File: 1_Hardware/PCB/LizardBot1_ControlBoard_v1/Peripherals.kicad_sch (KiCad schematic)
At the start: 30 parts, among them J501 Conn_01x03, J502 Conn_01x02, Q501 AO3400A, Q502 BSS138, Q503 BSS138, Q504 AO3400A, SW501 SW_Push, U501 MIC5225, U502 ICM-20948

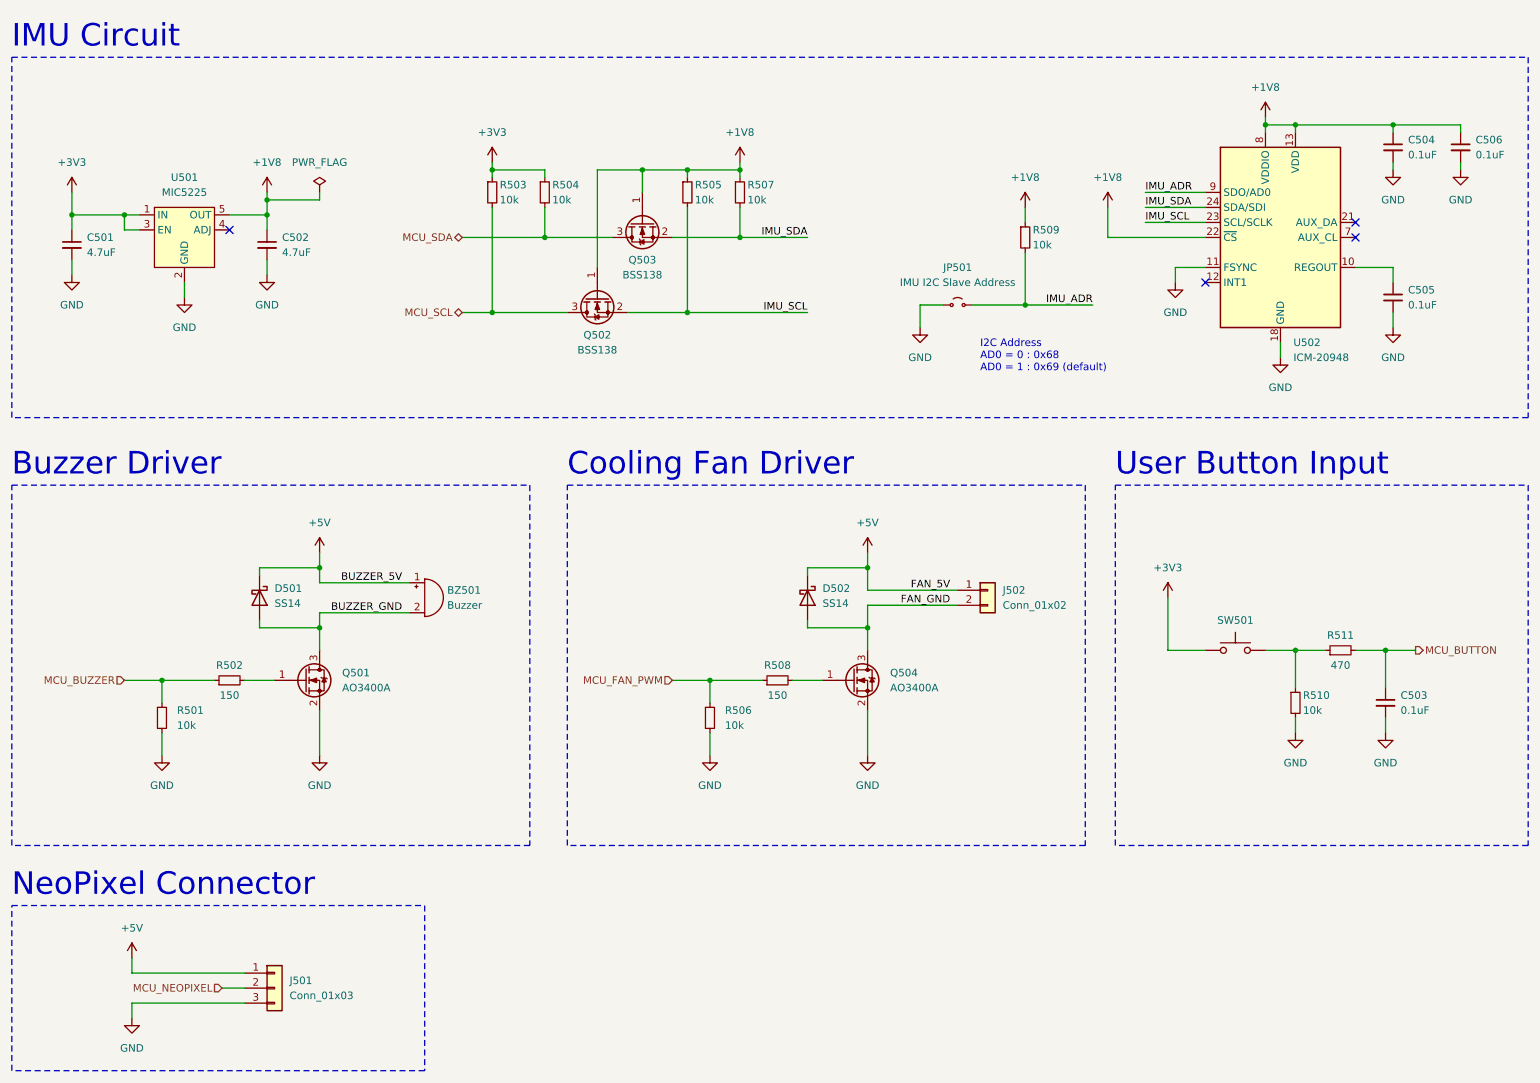
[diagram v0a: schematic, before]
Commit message: Added Communication_Interfaces schematic
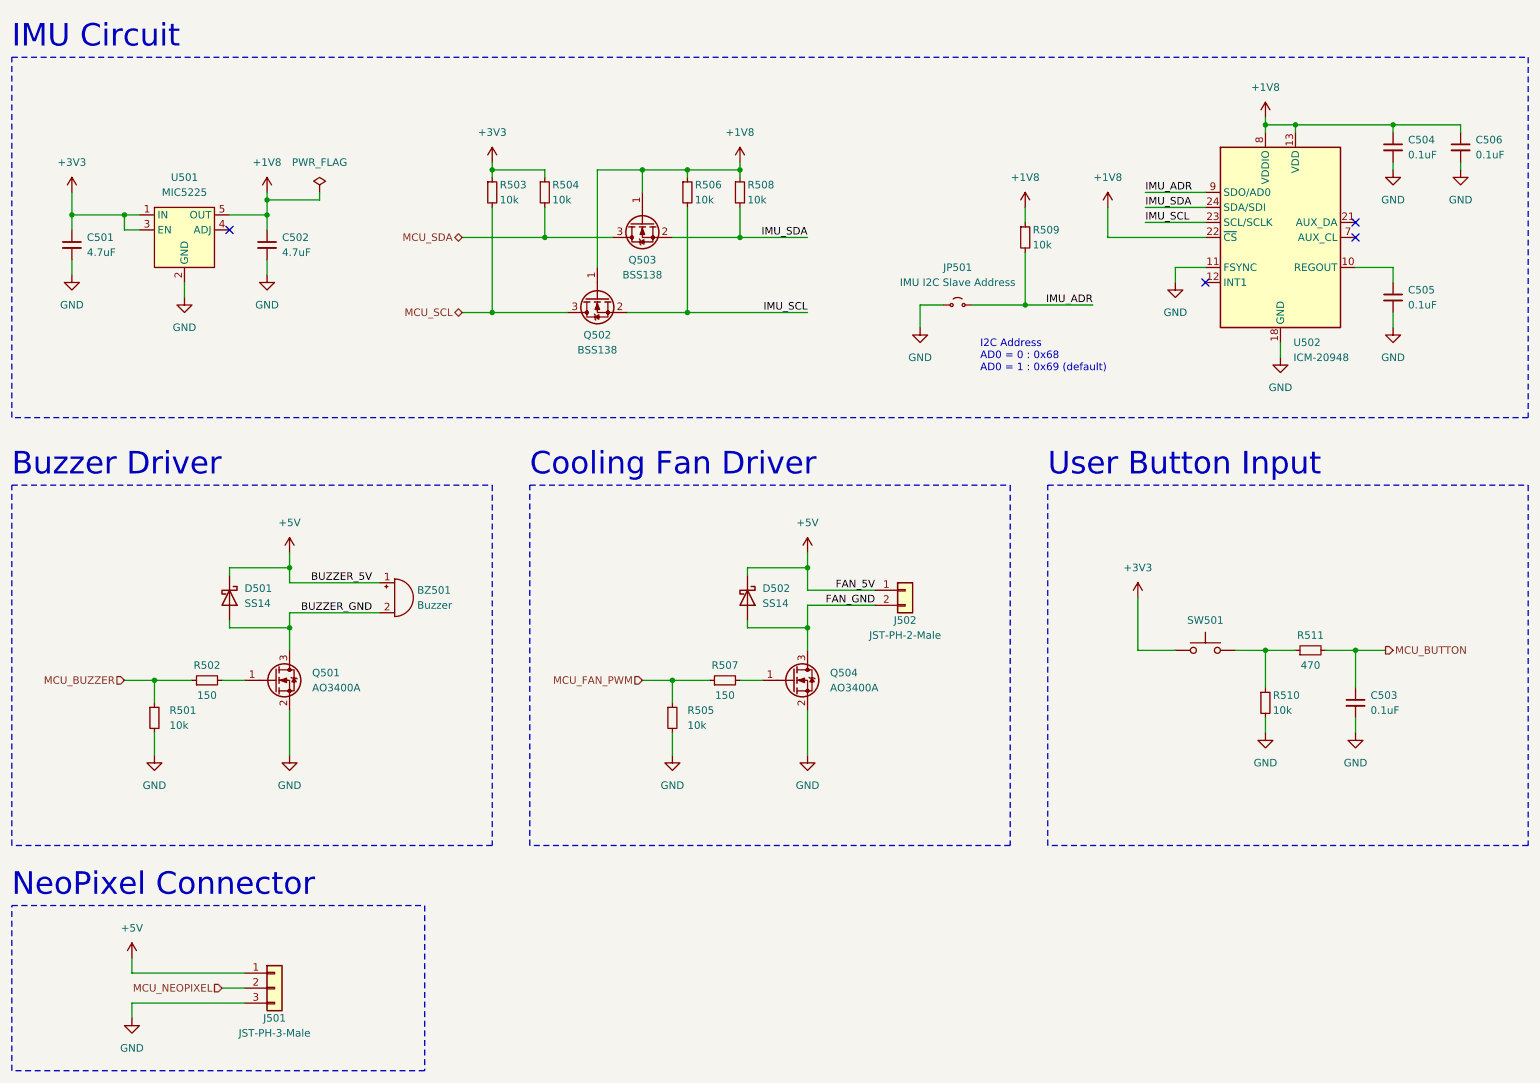
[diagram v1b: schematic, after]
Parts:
- removed R506: 10k, symbol Device:R_Small
- removed R508: 150, symbol Device:R_Small
- added R505: 10k, symbol Device:R_Small
- added R507: 150, symbol Device:R_Small
- J501: value Conn_01x03 -> JST-PH-3-Male
- J502: value Conn_01x02 -> JST-PH-2-Male
- renumbered R505 to R506, R507 to R508
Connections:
- net GND: now also R505.2
- net MCU_FAN_PWM: now also R505.1, R507.1
- net at Q504.1 (G): now also R507.2
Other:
- moved on the sheet: BZ501, C503, D501, D502, J502, Q501, Q504, R501, R502, R510, R511, SW501

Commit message: PCB schematics revision
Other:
- title: LizardBot 1 Control Board: Outputs -> LizardBot 1 Control Board: Peripherals

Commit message: Updated schematics. Assigned footprints. Added BOM to /4_Docs.
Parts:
- BZ501: footprint (none) -> Buzzer_Beeper:Buzzer_12x9.5RM7.6
- C501, C502: footprint (none) -> Capacitor_SMD:C_0805_2012Metric_Pad1.18x1.45mm_HandSolder
- C503, C504, C505, C506: footprint (none) -> Capacitor_SMD:C_0603_1608Metric_Pad1.08x0.95mm_HandSolder
- J501: footprint (none) -> Connector_JST:JST_PH_S3B-PH-K_1x03_P2.00mm_Horizontal
- J502: footprint (none) -> Connector_JST:JST_PH_S2B-PH-K_1x02_P2.00mm_Horizontal
- JP501: footprint (none) -> Jumper:SolderJumper-2_P1.3mm_Open_TrianglePad1.0x1.5mm
- R501, R502, R505, R507: footprint (none) -> Resistor_SMD:R_0805_2012Metric_Pad1.20x1.40mm_HandSolder
- R503, R504, R506, R508, R509, R510, R511: footprint (none) -> Resistor_SMD:R_0603_1608Metric_Pad0.98x0.95mm_HandSolder
- SW501: footprint (none) -> Button_Switch_THT:SW_PUSH-12mm
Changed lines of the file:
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@@
 			)
 		)
-		(property "Footprint" ""
+		(property "Footprint" "Buzzer_Beeper:Buzzer_12x9.5RM7.6"
 			(at 84.455 111.76 90)
 			(effects
@@
 			)
 		)
-		(property "Footprint" ""
+		(property "Footprint" "Resistor_SMD:R_0603_1608Metric_Pad0.98x0.95mm_HandSolder"
 			(at 240.03 123.19 0)
 			(effects
@@
 			)
 		)
-		(property "Footprint" ""
+		(property "Footprint" "Capacitor_SMD:C_0603_1608Metric_Pad1.08x0.95mm_HandSolder"
 			(at 254 38.1 0)
 			(effects
@@
 			)
 		)
-		(property "Footprint" ""
+		(property "Footprint" "Jumper:SolderJumper-2_P1.3mm_Open_TrianglePad1.0x1.5mm"
 			(at 180.34 64.77 0)
 			(effects
@@
 			)
 		)
-		(property "Footprint" ""
+		(property "Footprint" "Resistor_SMD:R_0603_1608Metric_Pad0.98x0.95mm_HandSolder"
 			(at 232.41 132.08 0)
 			(effects
@@
 			)
 		)
-		(property "Footprint" ""
+		(property "Footprint" "Button_Switch_THT:SW_PUSH-12mm"
 			(at 222.25 118.11 0)
 			(effects
@@
 			)
 		)
-		(property "Footprint" ""
+		(property "Footprint" "Capacitor_SMD:C_0603_1608Metric_Pad1.08x0.95mm_HandSolder"
 			(at 247.65 132.08 0)
 			(effects
@@
 			)
 		)
-		(property "Footprint" ""
+		(property "Footprint" "Resistor_SMD:R_0805_2012Metric_Pad1.20x1.40mm_HandSolder"
 			(at 140.97 128.27 0)
 			(effects
@@
 			)
 		)
-		(property "Footprint" ""
+		(property "Footprint" "Resistor_SMD:R_0603_1608Metric_Pad0.98x0.95mm_HandSolder"
 			(at 110.49 45.72 0)
 			(effects
@@
 			)
 		)
-		(property "Footprint" ""
+		(property "Footprint" "Capacitor_SMD:C_0805_2012Metric_Pad1.18x1.45mm_HandSolder"
 			(at 30.48 54.61 0)
 			(effects
@@
 			)
 		)
-		(property "Footprint" ""
+		(property "Footprint" "Resistor_SMD:R_0603_1608Metric_Pad0.98x0.95mm_HandSolder"
 			(at 191.77 53.34 0)
 			(effects
@@
 			)
 		)
-		(property "Footprint" ""
+		(property "Footprint" "Resistor_SMD:R_0603_1608Metric_Pad0.98x0.95mm_HandSolder"
 			(at 134.62 45.72 0)
 			(effects
@@
 			)
 		)
-		(property "Footprint" ""
+		(property "Footprint" "Resistor_SMD:R_0603_1608Metric_Pad0.98x0.95mm_HandSolder"
 			(at 101.6 45.72 0)
 			(effects
@@
 			)
 		)
-		(property "Footprint" ""
+		(property "Footprint" "Resistor_SMD:R_0805_2012Metric_Pad1.20x1.40mm_HandSolder"
 			(at 53.34 128.27 0)
 			(effects
@@
 			)
 		)
-		(property "Footprint" ""
+		(property "Footprint" "Connector_JST:JST_PH_S3B-PH-K_1x03_P2.00mm_Horizontal"
 			(at 64.77 180.34 0)
 			(effects
@@
 			)
 		)
-		(property "Footprint" ""
+		(property "Footprint" "Connector_JST:JST_PH_S2B-PH-K_1x02_P2.00mm_Horizontal"
 			(at 171.45 113.03 0)
 			(effects
@@
 			)
 		)
-		(property "Footprint" ""
+		(property "Footprint" "Resistor_SMD:R_0805_2012Metric_Pad1.20x1.40mm_HandSolder"
 			(at 44.45 134.62 0)
 			(effects
@@
 			)
 		)
-		(property "Footprint" ""
+		(property "Footprint" "Capacitor_SMD:C_0805_2012Metric_Pad1.18x1.45mm_HandSolder"
 			(at 63.5 54.61 0)
 			(effects
@@
 			)
 		)
-		(property "Footprint" ""
+		(property "Footprint" "Resistor_SMD:R_0805_2012Metric_Pad1.20x1.40mm_HandSolder"
 			(at 132.08 134.62 0)
 			(effects
@@
 			)
 		)
-		(property "Footprint" ""
+		(property "Footprint" "Capacitor_SMD:C_0603_1608Metric_Pad1.08x0.95mm_HandSolder"
 			(at 265.43 38.1 0)
 			(effects
@@
 			)
 		)
-		(property "Footprint" ""
+		(property "Footprint" "Capacitor_SMD:C_0603_1608Metric_Pad1.08x0.95mm_HandSolder"
 			(at 254 63.5 0)
 			(effects
@@
 			)
 		)
-		(property "Footprint" ""
+		(property "Footprint" "Resistor_SMD:R_0603_1608Metric_Pad0.98x0.95mm_HandSolder"
 			(at 143.51 45.72 0)
 			(effects

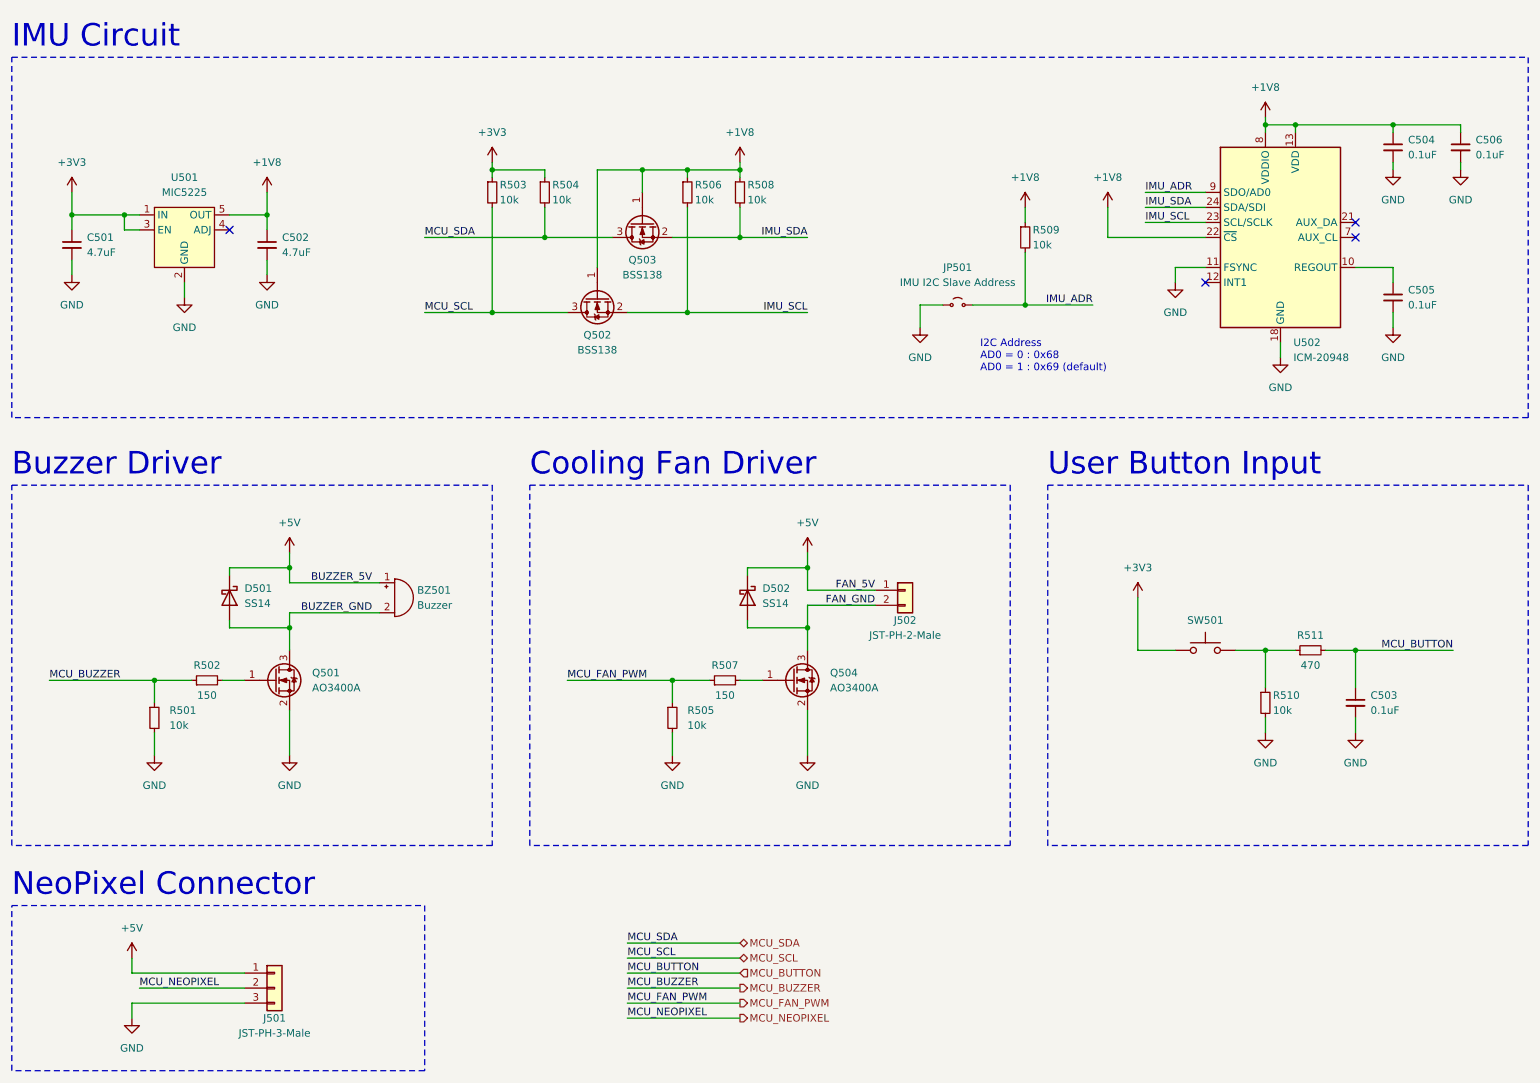
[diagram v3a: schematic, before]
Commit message: Added PCB Stack and Design Rules. Added PCB Layout file.
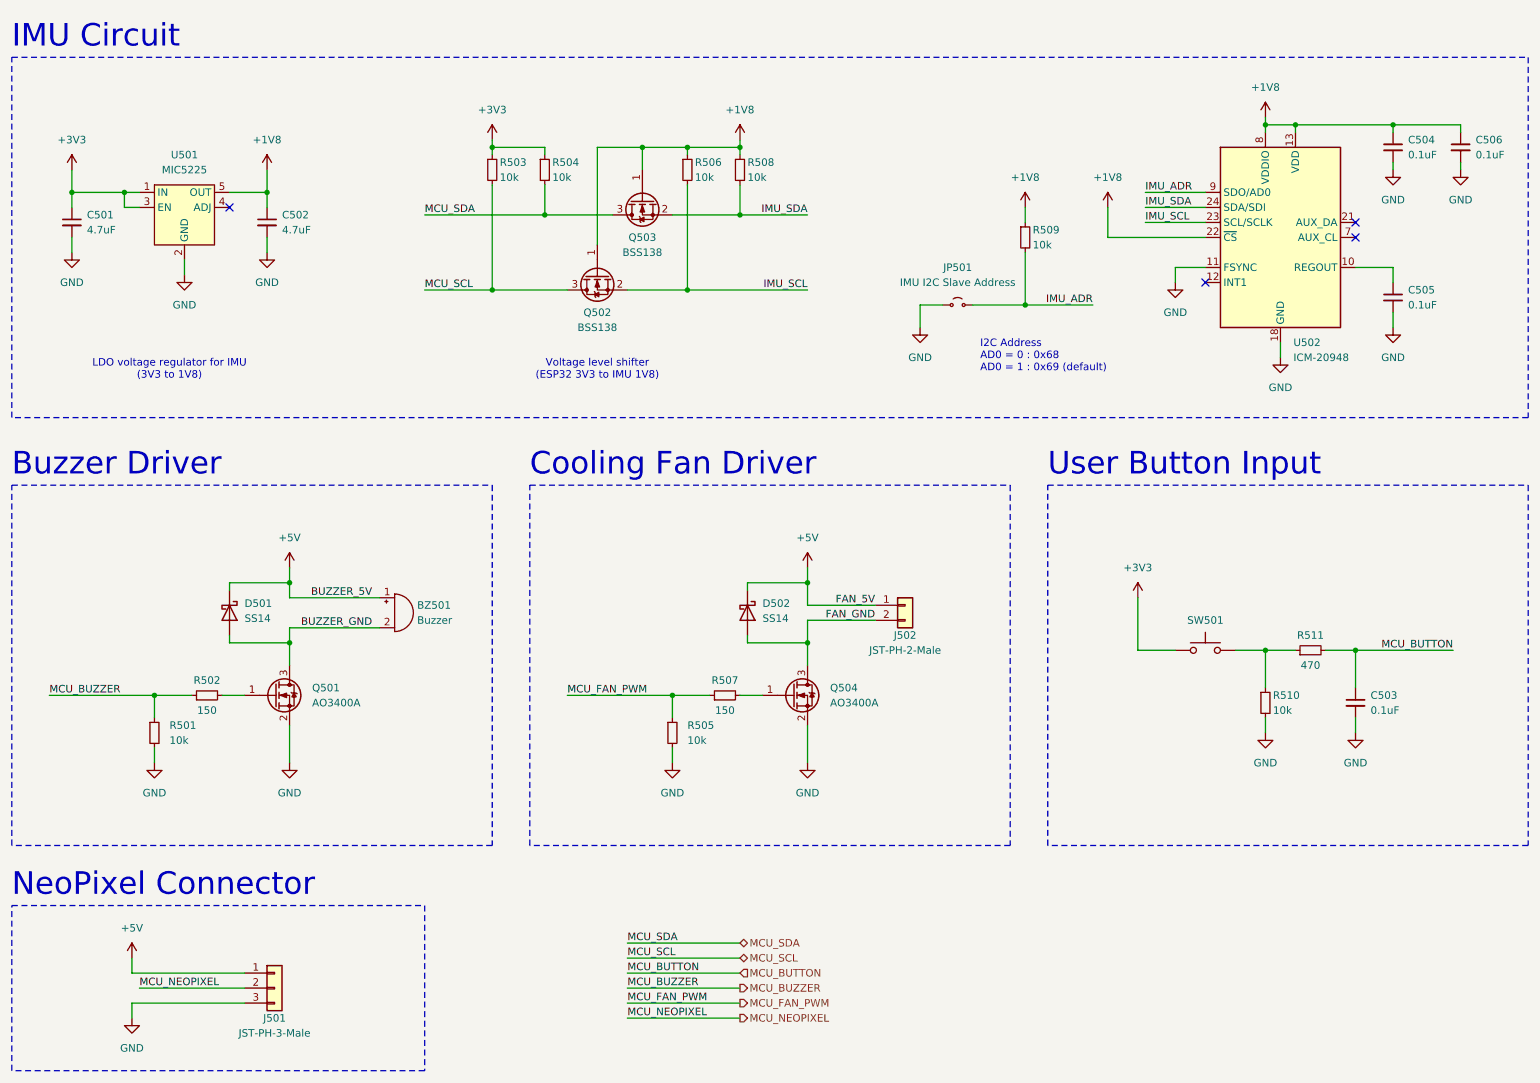
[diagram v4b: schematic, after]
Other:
- note added: "LDO voltage regulator for IMU (3V3 to 1V8)"
- note added: "Voltage level shifter (ESP32 3V3 to IMU 1V8)"
- moved on the sheet: BZ501, C501, C502, D501, D502, J502, Q501, Q502, Q503, Q504, R501, R502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

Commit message: Finished PCB routing. Updated ESP32 GPIO layout.
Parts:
- JP501: now left out of the parts list
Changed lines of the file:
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@@
 		(unit 1)
 		(exclude_from_sim yes)
-		(in_bom yes)
+		(in_bom no)
 		(on_board yes)
 		(dnp no)
